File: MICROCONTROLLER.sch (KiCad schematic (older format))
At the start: 14 parts, among them IC401 PIC16F1936

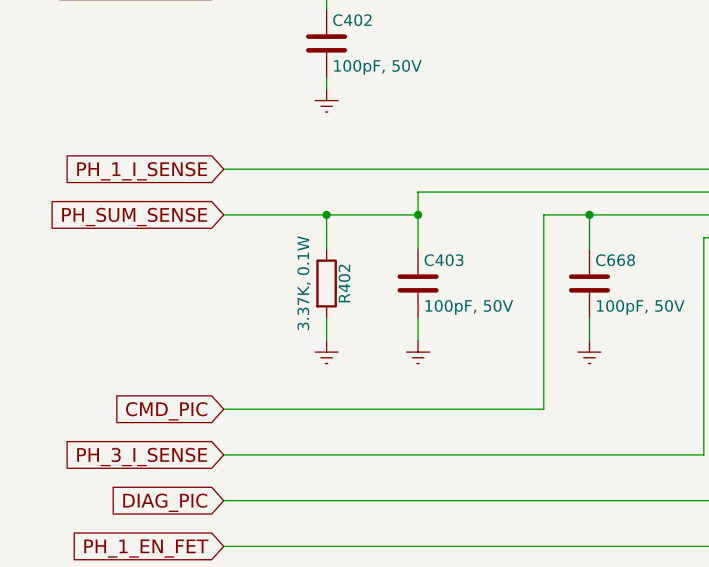
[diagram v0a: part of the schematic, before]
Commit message: - Finished traces.  Now copper areas.
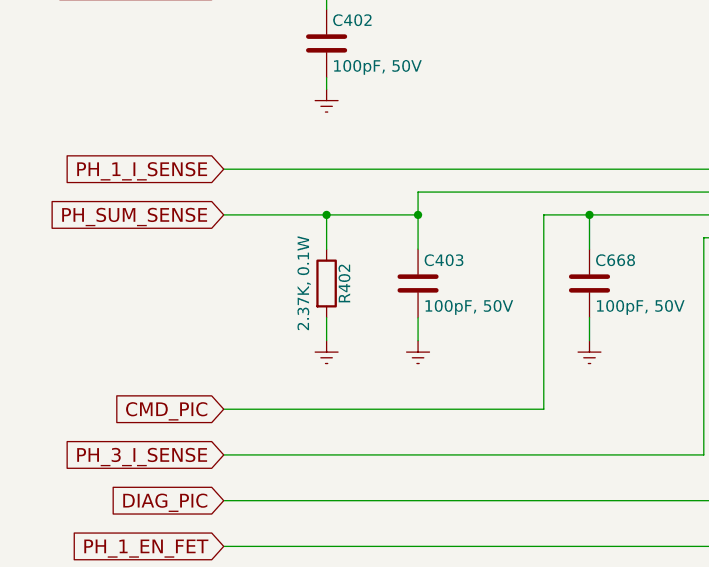
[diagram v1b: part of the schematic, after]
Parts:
- R402: value 3.37K, 0.1W -> 2.37K, 0.1W
- ST401: footprint (none) -> hp-bldc-pcb:HEADER_CONN_(FTM-106-02-L-DV)
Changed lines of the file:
@@
 P 2450 3450
 F 0 "R402" V 2530 3450 50  0000 C CNN
-F 1 "3.37K, 0.1W" V 2350 3450 50  0000 C CNN
+F 1 "2.37K, 0.1W" V 2350 3450 50  0000 C CNN
 F 2 "Resistors_SMD:R_0603" V 2380 3450 50  0001 C CNN
 F 3 "" H 2450 3450 50  0001 C CNN
@@
 F 0 "ST401" H 6000 5850 50  0000 C CNN
 F 1 "CONN_02X06" H 6000 5150 50  0001 C CNN
-F 2 "" H 6000 4300 50  0001 C CNN
+F 2 "hp-bldc-pcb:HEADER_CONN_(FTM-106-02-L-DV)" H 6000 4300 50  0001 C CNN
 F 3 "" H 6000 4300 50  0001 C CNN
 	1    6000 5500

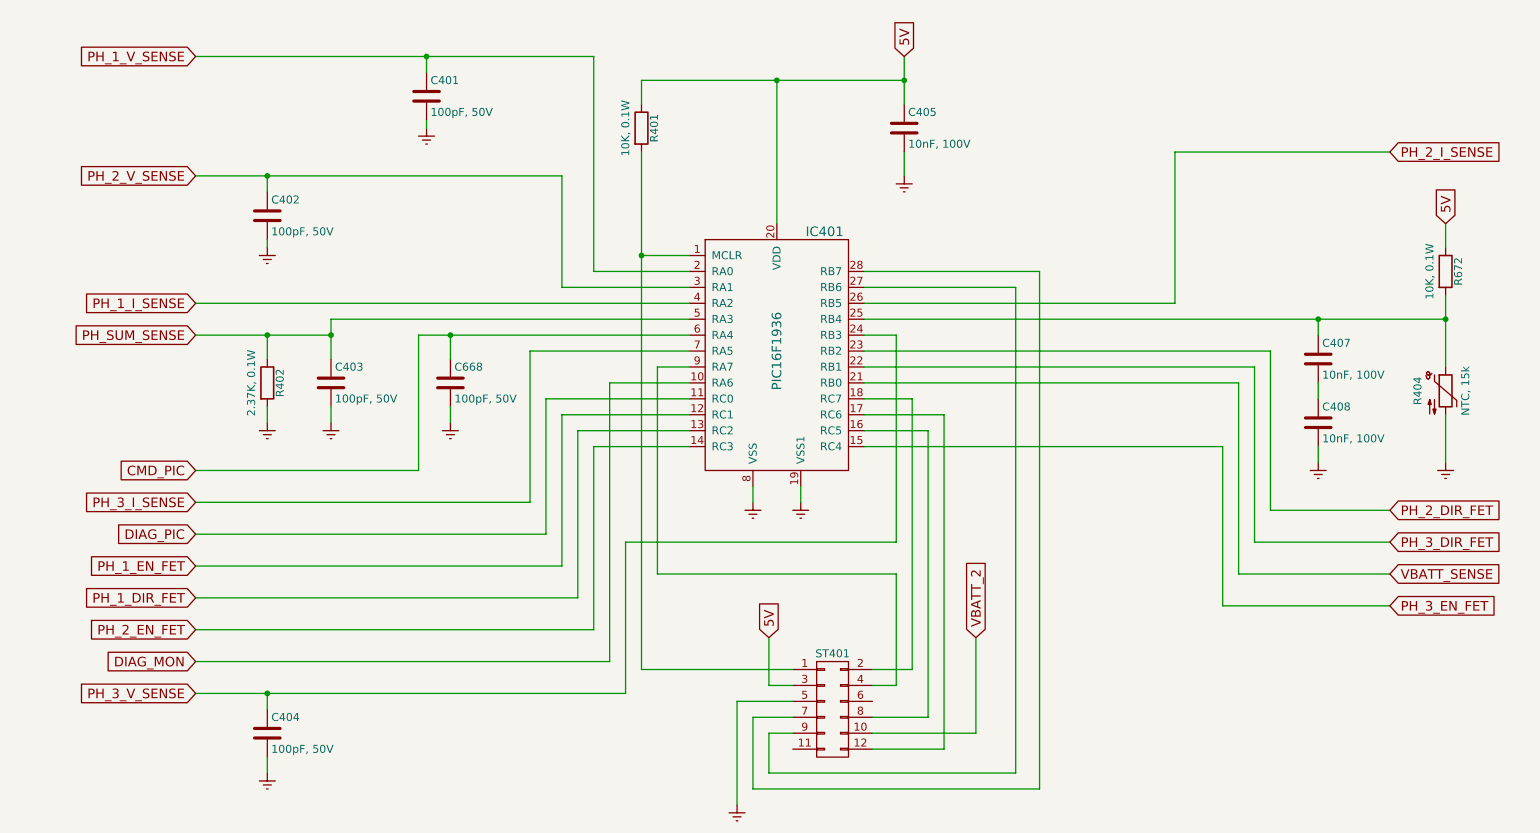
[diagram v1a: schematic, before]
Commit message: - Finished adaptation to JMS board footprint. - Added testpoints. - Changed header connector to 0.1" pitch, and tall.
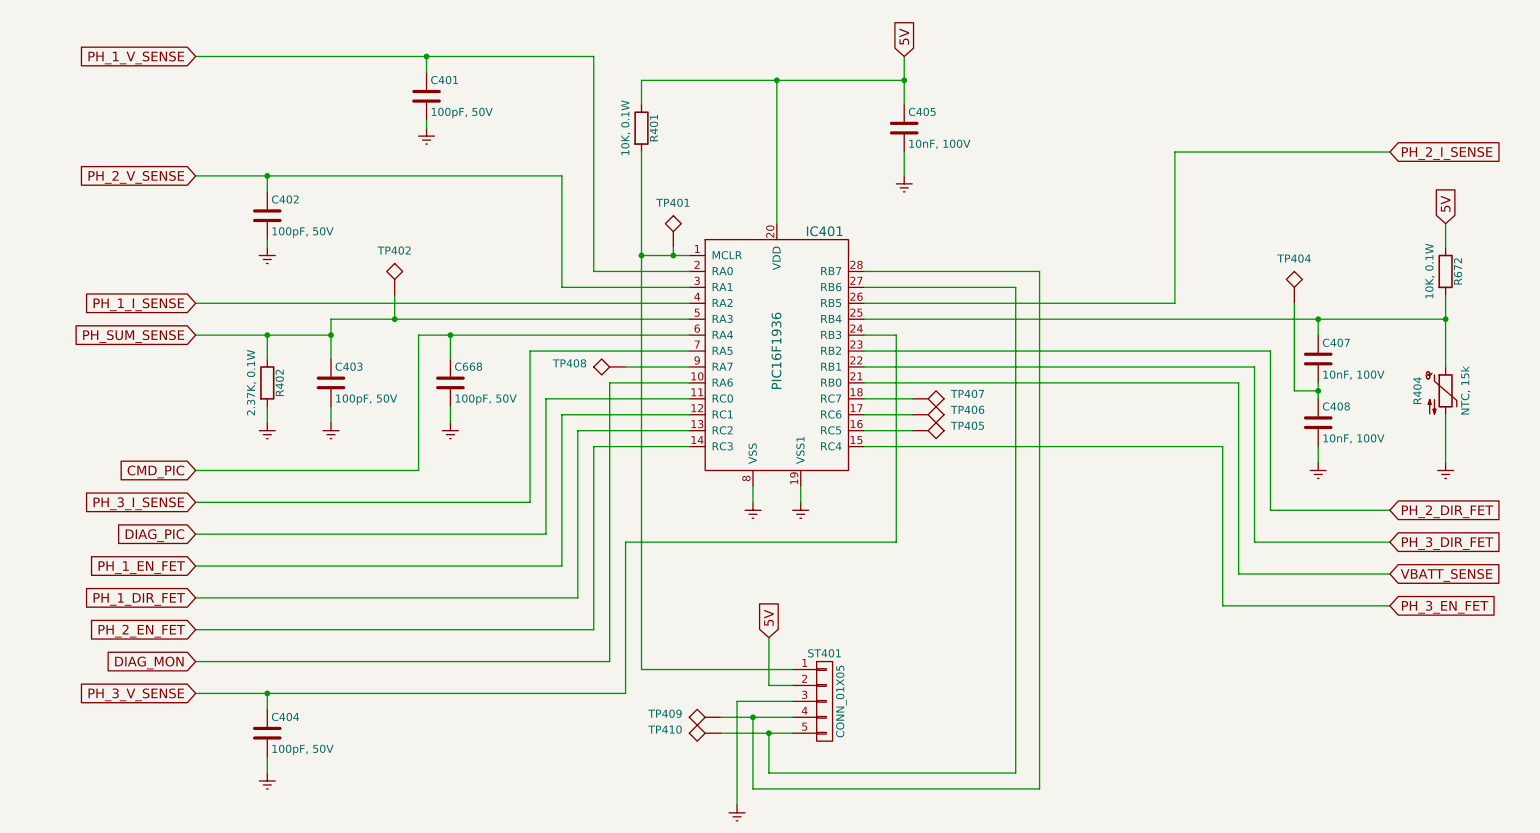
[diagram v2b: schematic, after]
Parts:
- removed ST401: CONN_02X06, hp-bldc-pcb:HEADER_CONN_(FTM-106-02-L-DV), symbol CONN_02X06
- added ST401: CONN_01X05, Pin_Headers:Pin_Header_Straight_1x05_Pitch2.54mm_SMD_Pin1Left, symbol CONN_01X05
- added TP401, TP402, TP404, TP405, TP406, TP407, TP408, TP409, TP410: TEST, hp-bldc-pcb:TEST_POINT_40mil, symbol TEST
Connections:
- net 5V: now also ST401.2 (P2)
- net Earth: now also ST401.3 (P3)
- net PH_SUM_SENSE: now also TP402.1
- net at IC401.1 (MCLR), R401.2: now also ST401.1 (P1), TP401.1
- net at IC401.16 (RC5): now also TP405.1
- net at IC401.17 (RC6): now also TP406.1
- net at IC401.18 (RC7): now also TP407.1
- net at IC401.27 (RB6): now also ST401.5 (P5), TP410.1
- net at IC401.28 (RB7): now also ST401.4 (P4), TP409.1
- net at IC401.9 (RA7): now also TP408.1
- net at C407.2, C408.1: now also TP404.1
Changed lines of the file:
@@
 5V
 $Comp
-L Earth #PWR025
+L Earth #PWR026
 U 1 1 5A798686
 P 6450 2150
-F 0 "#PWR025" H 6450 1900 50  0001 C CNN
+F 0 "#PWR026" H 6450 1900 50  0001 C CNN
 F 1 "Earth" H 6450 2000 50  0001 C CNN
 F 2 "" H 6450 2150 50  0001 C CNN
@@
 PH_1_V_SENSE
 $Comp
-L Earth #PWR026
+L Earth #PWR027
 U 1 1 5A79A192
 P 3450 1850
-F 0 "#PWR026" H 3450 1600 50  0001 C CNN
+F 0 "#PWR027" H 3450 1600 50  0001 C CNN
 F 1 "Earth" H 3450 1700 50  0001 C CNN
 F 2 "" H 3450 1850 50  0001 C CNN
@@
 $EndComp
 $Comp
-L Earth #PWR027
+L Earth #PWR028
 U 1 1 5A79A215
 P 2450 2600
-F 0 "#PWR027" H 2450 2350 50  0001 C CNN
+F 0 "#PWR028" H 2450 2350 50  0001 C CNN
 F 1 "Earth" H 2450 2450 50  0001 C CNN
 F 2 "" H 2450 2600 50  0001 C CNN
@@
 $EndComp
 $Comp
-L Earth #PWR028
+L Earth #PWR029
 U 1 1 5A79A4CB
 P 2450 3700
-F 0 "#PWR028" H 2450 3450 50  0001 C CNN
+F 0 "#PWR029" H 2450 3450 50  0001 C CNN
 F 1 "Earth" H 2450 3550 50  0001 C CNN
 F 2 "" H 2450 3700 50  0001 C CNN
@@
 $EndComp
 $Comp
-L Earth #PWR029
+L Earth #PWR030
 U 1 1 5A79A594
 P 2850 3700
-F 0 "#PWR029" H 2850 3450 50  0001 C CNN
+F 0 "#PWR030" H 2850 3450 50  0001 C CNN
 F 1 "Earth" H 2850 3550 50  0001 C CNN
 F 2 "" H 2850 3700 50  0001 C CNN
@@
 $EndComp
 $Comp
-L Earth #PWR030
+L Earth #PWR031
 U 1 1 5A79A998
 P 3600 3700
-F 0 "#PWR030" H 3600 3450 50  0001 C CNN
+F 0 "#PWR031" H 3600 3450 50  0001 C CNN
 F 1 "Earth" H 3600 3550 50  0001 C CNN
 F 2 "" H 3600 3700 50  0001 C CNN
@@
 DIAG_MON
 $Comp
-L Earth #PWR031
+L Earth #PWR032
 U 1 1 5A79AE58
 P 5500 4200
-F 0 "#PWR031" H 5500 3950 50  0001 C CNN
+F 0 "#PWR032" H 5500 3950 50  0001 C CNN
 F 1 "Earth" H 5500 4050 50  0001 C CNN
 F 2 "" H 5500 4200 50  0001 C CNN
@@
 $EndComp
 $Comp
-L Earth #PWR032
+L Earth #PWR033
 U 1 1 5A79AE7B
 P 5800 4200
-F 0 "#PWR032" H 5800 3950 50  0001 C CNN
+F 0 "#PWR033" H 5800 3950 50  0001 C CNN
 F 1 "Earth" H 5800 4050 50  0001 C CNN
 F 2 "" H 5800 4200 50  0001 C CNN
@@
 $EndComp
 $Comp
-L Earth #PWR033
+L Earth #PWR034
 U 1 1 5A79B16D
 P 2450 5900
-F 0 "#PWR033" H 2450 5650 50  0001 C CNN
+F 0 "#PWR034" H 2450 5650 50  0001 C CNN
 F 1 "Earth" H 2450 5750 50  0001 C CNN
 F 2 "" H 2450 5900 50  0001 C CNN
@@
 $EndComp
 $Comp
-L Earth #PWR034
+L Earth #PWR035
 U 1 1 5A79B922
 P 9850 3950
-F 0 "#PWR034" H 9850 3700 50  0001 C CNN
+F 0 "#PWR035" H 9850 3700 50  0001 C CNN
 F 1 "Earth" H 9850 3800 50  0001 C CNN
 F 2 "" H 9850 3950 50  0001 C CNN
@@
 $EndComp
 $Comp
-L Earth #PWR035
+L Earth #PWR036
 U 1 1 5A79BAEE
 P 9050 3950
-F 0 "#PWR035" H 9050 3700 50  0001 C CNN
+F 0 "#PWR036" H 9050 3700 50  0001 C CNN
 F 1 "Earth" H 9050 3800 50  0001 C CNN
 F 2 "" H 9050 3950 50  0001 C CNN
@@
 Wire Wire Line
 	6400 3150 6200 3150
-$Comp
-L CONN_02X06 ST401
-U 1 1 5A79C910
-P 6000 5500
-F 0 "ST401" H 6000 5850 50  0000 C CNN
-F 1 "CONN_02X06" H 6000 5150 50  0001 C CNN
-F 2 "hp-bldc-pcb:HEADER_CONN_(FTM-106-02-L-DV)" H 6000 4300 50  0001 C CNN
-F 3 "" H 6000 4300 50  0001 C CNN
-	1    6000 5500
-	1    0    0    -1
-$EndComp
 Wire Wire Line
 	4800 5250 5750 5250
@@
 	5600 5350 5600 5050
 $Comp
-L Earth #PWR036
+L Earth #PWR037
 U 1 1 5A79CAEE
 P 5400 6100
-F 0 "#PWR036" H 5400 5850 50  0001 C CNN
+F 0 "#PWR037" H 5400 5850 50  0001 C CNN
 F 1 "Earth" H 5400 5950 50  0001 C CNN
 F 2 "" H 5400 6100 50  0001 C CNN
@@
 $EndComp
 Wire Wire Line
-	5750 5650 5600 5650
+	5300 5650 5750 5650
 Wire Wire Line
 	5600 5650 5600 5900
@@
 	7150 2850 6200 2850
 Wire Wire Line
-	5750 5550 5500 5550
+	5300 5550 5750 5550
 Wire Wire Line
 	5500 5550 5500 6000
@@
 	7300 2750 6200 2750
 Wire Wire Line
-	6250 5250 6500 5250
-Wire Wire Line
-	6500 5250 6500 3550
-Wire Wire Line
-	6500 3550 6200 3550
-Wire Wire Line
-	6250 5550 6600 5550
-Wire Wire Line
-	6600 5550 6600 3750
-Wire Wire Line
-	6600 3750 6200 3750
-Wire Wire Line
-	6250 5750 6700 5750
-Wire Wire Line
-	6700 5750 6700 3650
-Wire Wire Line
-	6700 3650 6200 3650
-Wire Wire Line
-	6250 5350 6400 5350
-Wire Wire Line
-	6400 5350 6400 4650
-Wire Wire Line
-	6400 4650 4900 4650
-Wire Wire Line
-	4900 4650 4900 3350
-Wire Wire Line
-	4900 3350 5100 3350
-Wire Wire Line
 	5750 5450 5400 5450
 Wire Wire Line
 	5400 5450 5400 6100
-Text GLabel 6900 5050 1    60   Input ~ 0
-VBATT_2
-Wire Wire Line
-	6250 5650 6900 5650
-Wire Wire Line
-	6900 5650 6900 5050
+$Comp
+L CONN_01X05 ST401
+U 1 1 5AAA779F
+P 5950 5450
+F 0 "ST401" H 5950 5750 50  0000 C CNN
+F 1 "CONN_01X05" V 6050 5450 50  0000 C CNN
+F 2 "Pin_Headers:Pin_Header_Straight_1x05_Pitch2.54mm_SMD_Pin1Left" H 5950 5450 50  0001 C CNN
+F 3 "" H 5950 5450 50  0001 C CNN
+	1    5950 5450
+	1    0    0    -1
+$EndComp
+$Comp
+L TEST TP401
+U 1 1 5AB3978D
+P 5000 2600
+F 0 "TP401" H 5000 2850 50  0000 C BNN
+F 1 "TEST" H 5000 2850 50  0001 C CNN
+F 2 "hp-bldc-pcb:TEST_POINT_40mil" H 5000 2600 50  0001 C CNN
+F 3 "" H 5000 2600 50  0001 C CNN
+	1    5000 2600
+	1    0    0    -1
+$EndComp
+Wire Wire Line
+	5000 2600 5000 2650
+Connection ~ 5000 2650
+$Comp
+L TEST TP402
+U 1 1 5AB39913
+P 3250 2900
+F 0 "TP402" H 3250 3150 50  0000 C BNN
+F 1 "TEST" H 3250 3150 50  0001 C CNN
+F 2 "hp-bldc-pcb:TEST_POINT_40mil" H 3250 2900 50  0001 C CNN
+F 3 "" H 3250 2900 50  0001 C CNN
+	1    3250 2900
+	1    0    0    -1
+$EndComp
+Wire Wire Line
+	3250 2900 3250 3050
+Connection ~ 3250 3050
+$Comp
+L TEST TP408
+U 1 1 5AB39A37
+P 4700 3350
+F 0 "TP408" V 4750 3700 50  0000 C BNN
+F 1 "TEST" H 4700 3600 50  0001 C CNN
+F 2 "hp-bldc-pcb:TEST_POINT_40mil" H 4700 3350 50  0001 C CNN
+F 3 "" H 4700 3350 50  0001 C CNN
+	1    4700 3350
+	0    -1   -1   0
+$EndComp
+Wire Wire Line
+	4700 3350 5100 3350
+$Comp
+L TEST TP407
+U 1 1 5AB3A058
+P 6500 3550
+F 0 "TP407" V 6500 3900 50  0000 C BNN
+F 1 "TEST" H 6500 3800 50  0001 C CNN
+F 2 "hp-bldc-pcb:TEST_POINT_40mil" H 6500 3550 50  0001 C CNN
+F 3 "" H 6500 3550 50  0001 C CNN
+	1    6500 3550
+	0    1    1    0
+$EndComp
+$Comp
+L TEST TP406
+U 1 1 5AB3A124
+P 6500 3650
+F 0 "TP406" V 6500 4000 50  0000 C BNN
+F 1 "TEST" H 6500 3900 50  0001 C CNN
+F 2 "hp-bldc-pcb:TEST_POINT_40mil" H 6500 3650 50  0001 C CNN
+F 3 "" H 6500 3650 50  0001 C CNN
+	1    6500 3650
+	0    1    1    0
+$EndComp
+$Comp
+L TEST TP405
+U 1 1 5AB3A16D
+P 6500 3750
+F 0 "TP405" V 6500 4100 50  0000 C BNN
+F 1 "TEST" H 6500 4000 50  0001 C CNN
+F 2 "hp-bldc-pcb:TEST_POINT_40mil" H 6500 3750 50  0001 C CNN
+F 3 "" H 6500 3750 50  0001 C CNN
+	1    6500 3750
+	0    1    1    0
+$EndComp
+Wire Wire Line
+	6200 3550 6500 3550
+Wire Wire Line
+	6200 3650 6500 3650
+Wire Wire Line
+	6200 3750 6500 3750
+$Comp
+L TEST TP409
+U 1 1 5AB3A5AC
+P 5300 5550
+F 0 "TP409" V 5350 5900 50  0000 C BNN
+F 1 "TEST" H 5300 5800 50  0001 C CNN
+F 2 "hp-bldc-pcb:TEST_POINT_40mil" H 5300 5550 50  0001 C CNN
+F 3 "" H 5300 5550 50  0001 C CNN
+	1    5300 5550
+	0    -1   -1   0
+$EndComp
+$Comp
+L TEST TP410
+U 1 1 5AB3A639
+P 5300 5650
+F 0 "TP410" V 5350 6000 50  0000 C BNN
+F 1 "TEST" H 5300 5900 50  0001 C CNN
+F 2 "hp-bldc-pcb:TEST_POINT_40mil" H 5300 5650 50  0001 C CNN
+F 3 "" H 5300 5650 50  0001 C CNN
+	1    5300 5650
+	0    -1   -1   0
+$EndComp
+Connection ~ 5500 5550
+Connection ~ 5600 5650
+$Comp
+L TEST TP404
+U 1 1 5AB3A800
+P 8900 2950
+F 0 "TP404" H 8900 3200 50  0000 C BNN
+F 1 "TEST" H 8900 3200 50  0001 C CNN
+F 2 "hp-bldc-pcb:TEST_POINT_40mil" H 8900 2950 50  0001 C CNN
+F 3 "" H 8900 2950 50  0001 C CNN
+	1    8900 2950
+	1    0    0    -1
+$EndComp
+Wire Wire Line
+	8900 2950 8900 3500
+Wire Wire Line
+	8900 3500 9050 3500
+Connection ~ 9050 3500
 $EndSCHEMATC

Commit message: - Minor changes to silkscreen. - Minor changes to BOM. - Additions to Readme file. - Page layout changed in schematic.
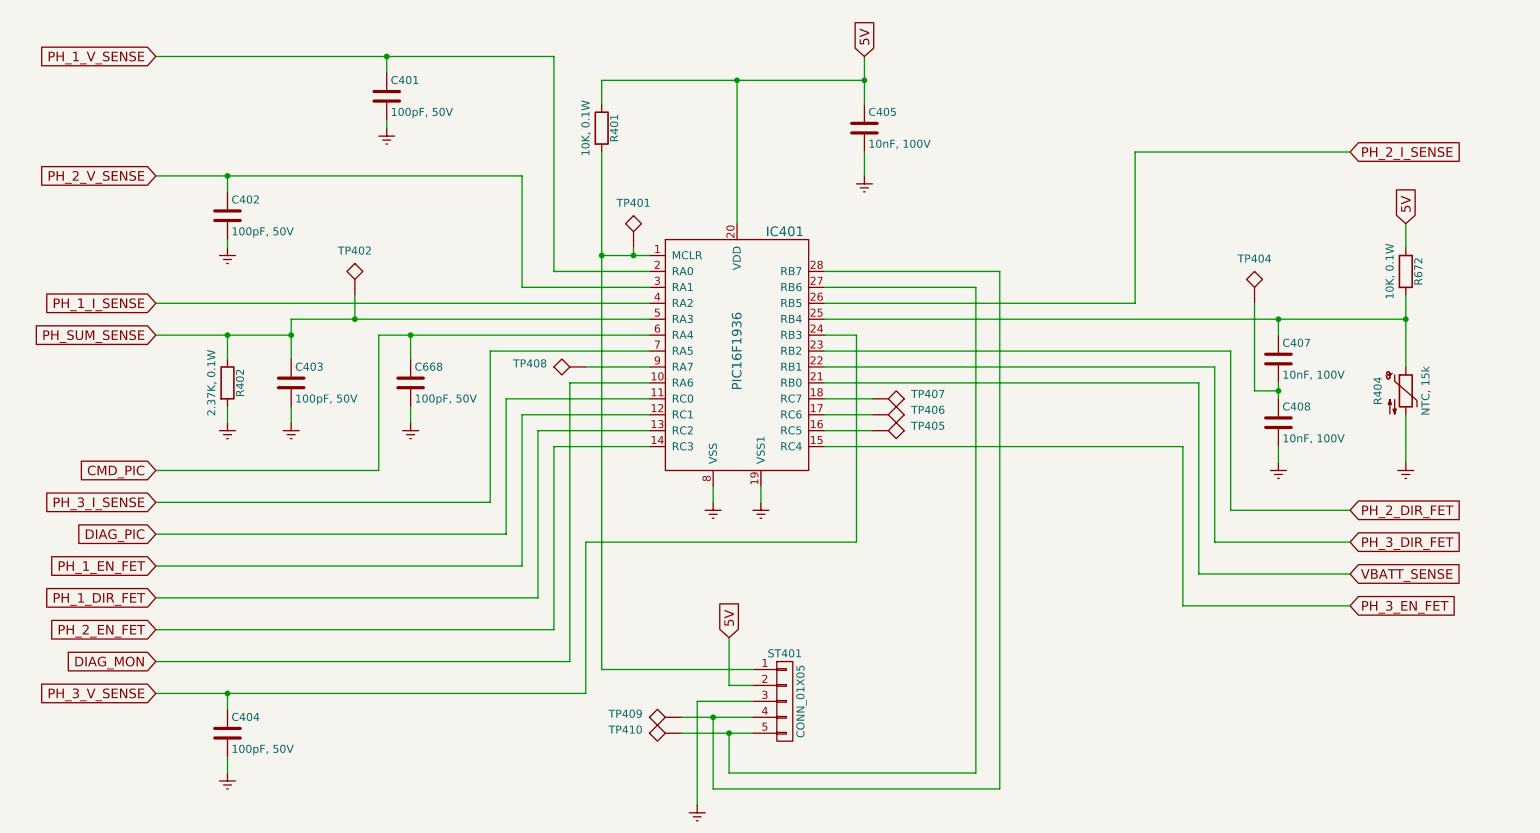
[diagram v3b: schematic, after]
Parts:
- ST401: footprint Pin_Headers:Pin_Header_Straight_1x05_Pitch2.54mm_SMD_Pin1Left -> hp-bldc-pcb:Pin_Header_Straight_1x05_Pitch2.54mm_SMD_Pin1Left
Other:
- moved on the sheet: C401, C402, C403, C404, C405, C407, C408, C668, IC401, R401, R402, R404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

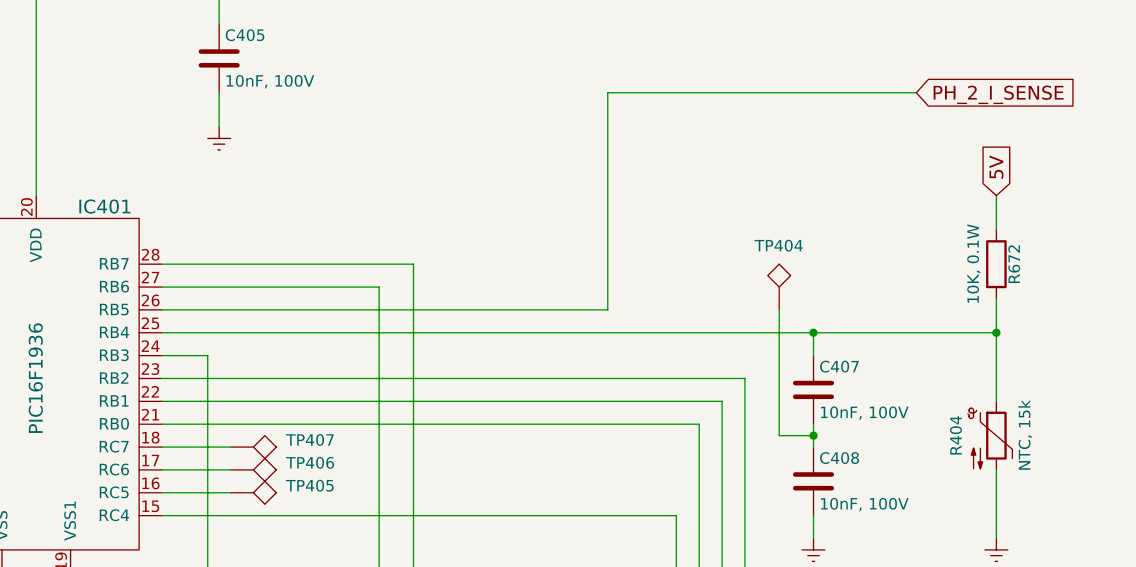
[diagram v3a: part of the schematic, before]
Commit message: - Added TP411 at JMS request.  This was needed to test the NTC during ICT.
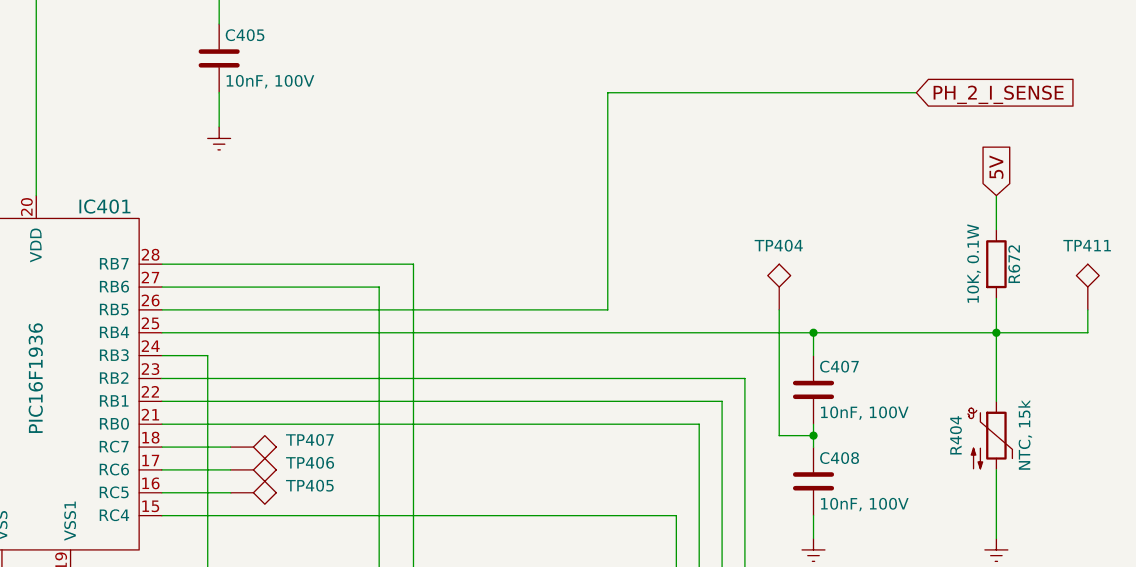
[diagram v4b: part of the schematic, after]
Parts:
- added TP411: TEST, hp-bldc-pcb:TEST_POINT_40mil, symbol TEST
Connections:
- net at C407.1, IC401.25 (RB4), R404.1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: now also TP411.1
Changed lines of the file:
@@
 	9600 2450 9600 2600
 Wire Wire Line
-	5950 3050 9600 3050
+	5950 3050 10000 3050
 Wire Wire Line
 	9600 2900 9600 3350
@@
 	8650 3500 8800 3500
 Connection ~ 8800 3500
+$Comp
+L TEST TP411
+U 1 1 5BBB7BCC
+P 10000 2950
+F 0 "TP411" H 10000 3200 50  0000 C BNN
+F 1 "TEST" H 10000 3200 50  0001 C CNN
+F 2 "hp-bldc-pcb:TEST_POINT_40mil" H 10000 2950 50  0001 C CNN
+F 3 "" H 10000 2950 50  0001 C CNN
+	1    10000 2950
+	1    0    0    -1
+$EndComp
+Wire Wire Line
+	10000 3050 10000 2950
 $EndSCHEMATC
